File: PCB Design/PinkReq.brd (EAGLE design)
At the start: 53.3 x 66 mm, 7 parts

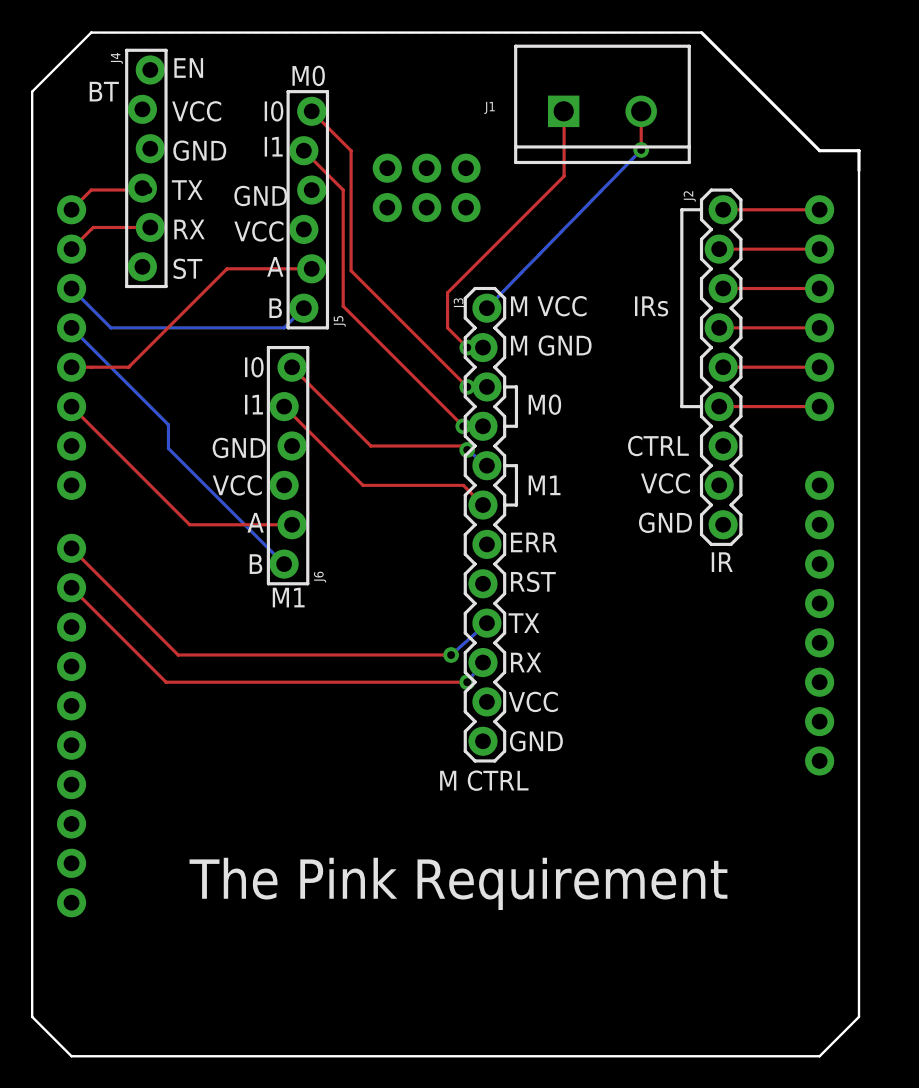
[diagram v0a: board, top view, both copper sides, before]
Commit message: PCB updated with SR04
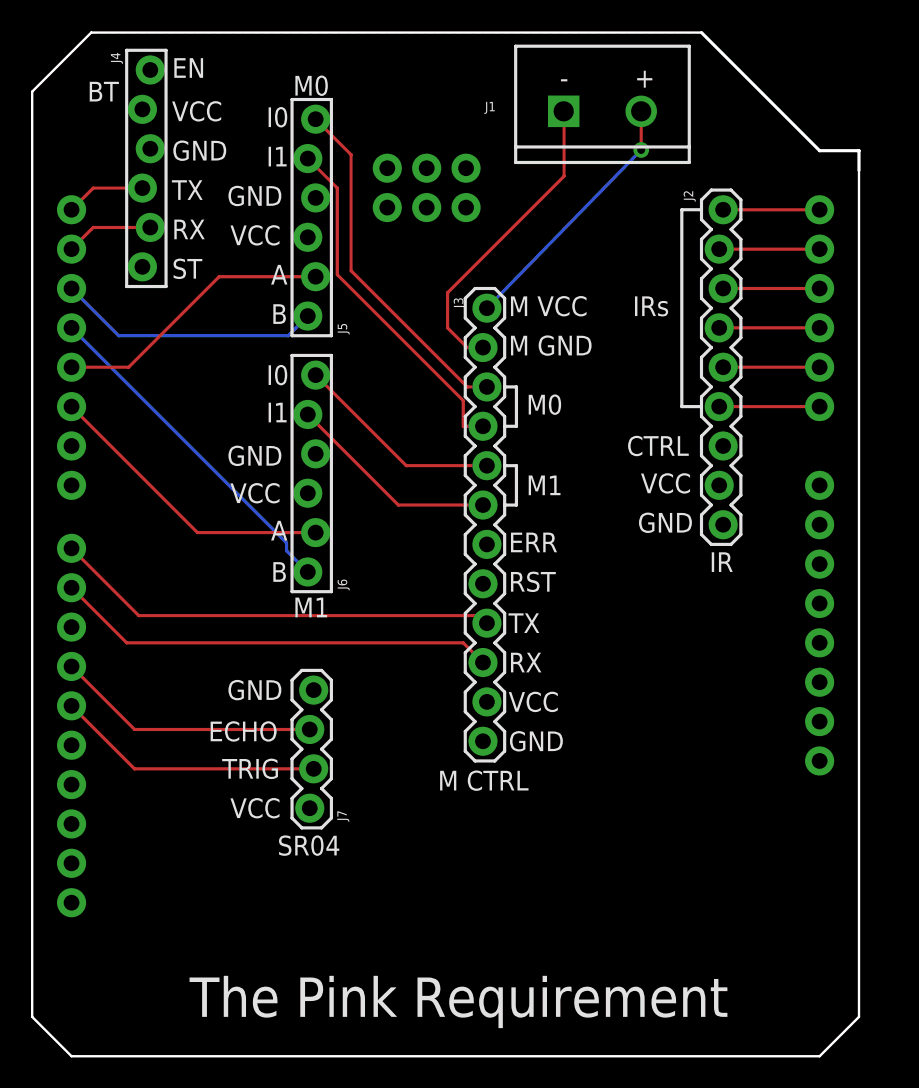
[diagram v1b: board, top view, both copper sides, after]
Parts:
- added J7: (no value), SparkFun-Connectors:1X04_LOCK
- moved J6 1.61 mm to (18.0, 31.2)
- moved J5 0.57 mm to (18.0, 47.8)
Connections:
- new net ECHO: B1.D11, J7.2
- new net TRIG: B1.D12, J7.3
- net GND: now also J7.1
- net VCC: now also J7.4
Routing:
- net TRIG: track 0.00 -> 17.3 mm
- net ECHO: track 0.00 -> 17.1 mm
- net M10: track 15.3 -> 13.5 mm, vias 1 -> 0
- net 1A: track 17.4 -> 19.1 mm
- net M11: track 15.5 -> 13.7 mm
- net MTX: track 30.4 -> 28.8 mm, vias 1 -> 0
- net 1B: track 20.9 -> 22.1 mm
- net MRX: track 29.7 -> 28.5 mm, vias 1 -> 0
- net BTX: track 5.88 -> 5.15 mm, vias 1 -> 0
- net M00: track 23.2 -> 22.6 mm, vias 1 -> 0
- net M01: track 23.3 -> 22.7 mm, vias 1 -> 0
- net MGND: vias 1 -> 0
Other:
- board text added: "+"
- board text added: "-"
- board text added: "ECHO"
- board text added: "SR04"
- board text added: "TRIG"

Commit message: PCB and Qik w/ BT added
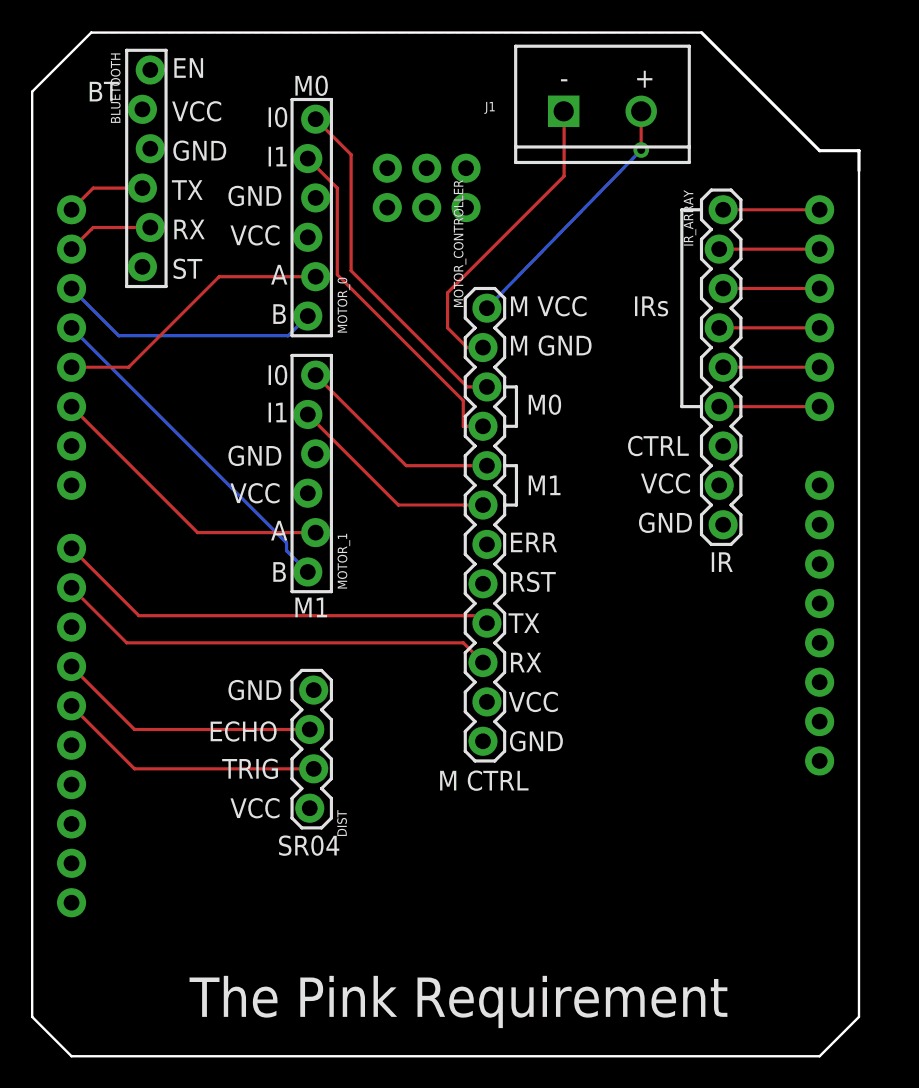
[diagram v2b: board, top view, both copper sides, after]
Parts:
- renumbered J2 to IR_ARRAY, J3 to MOTOR_CONTROLLER, J4 to BLUETOOTH, J5 to MOTOR_0, J6 to MOTOR_1, J7 to DIST
